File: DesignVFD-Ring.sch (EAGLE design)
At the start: 31 parts, among them IC1 LMR64010XMF/NOPB, IC2 LM340S-05, J1 NPPN081BFLD-RC, J2 NPPN081BFLD-RC, J3 NPPN081BFLD-RC, J4 NPPN081BFLD-RC, U1 MAX6920AWP+, U2 LM1084IS-5.0, U3 TPS76325DBVT

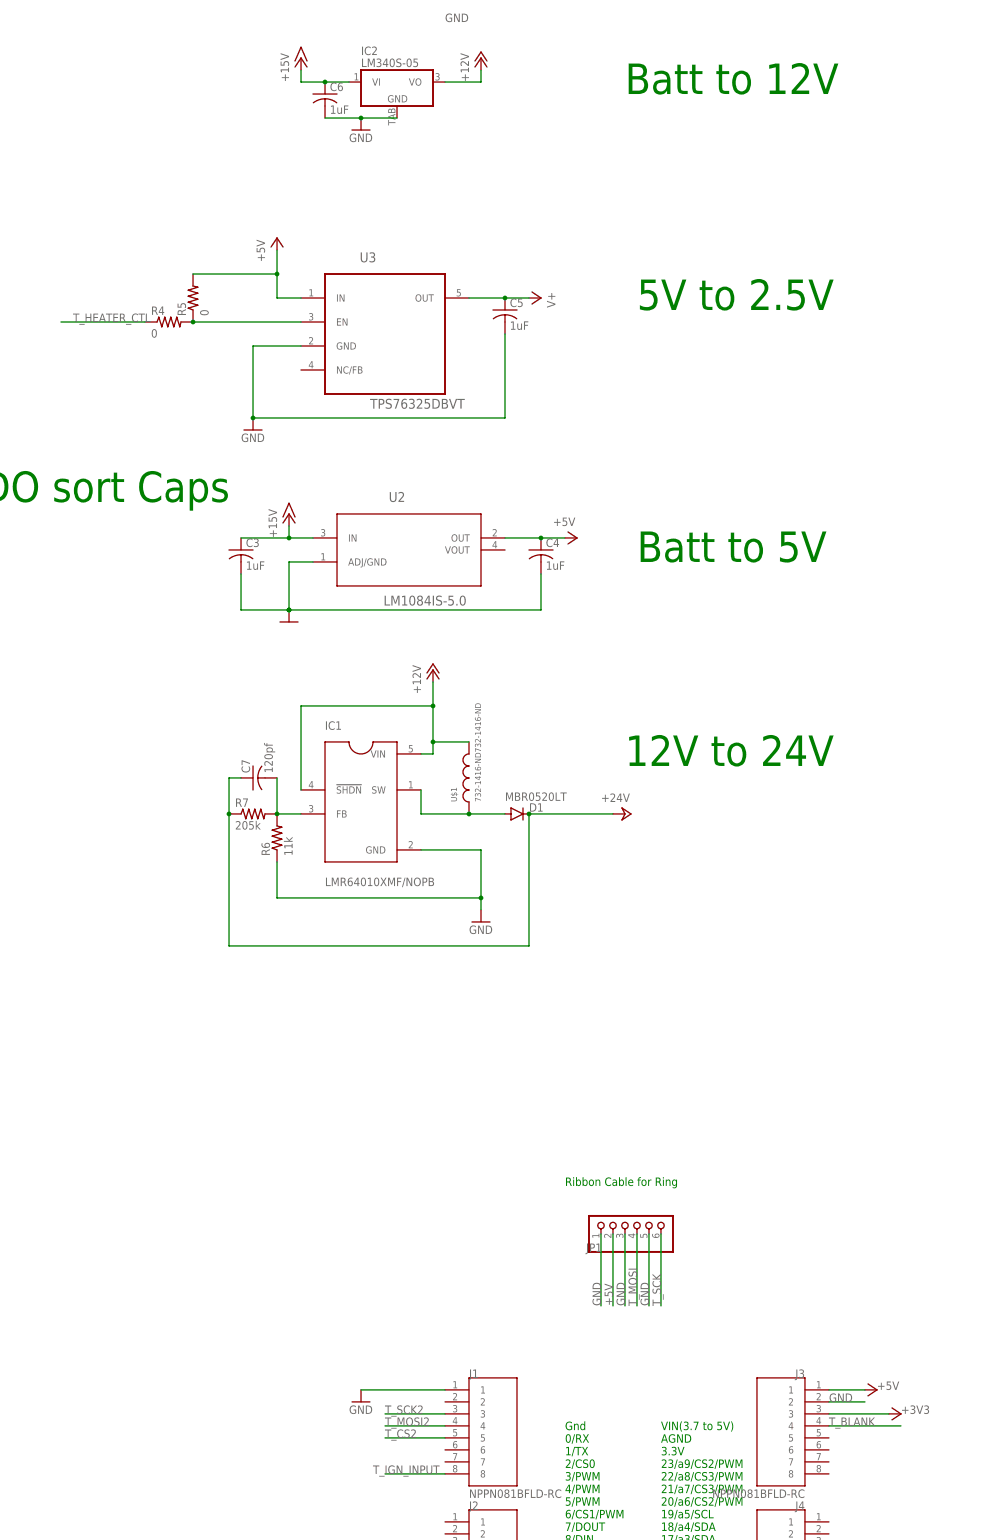
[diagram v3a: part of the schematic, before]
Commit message: added 7th ribbon cable connection, verified SMPS values
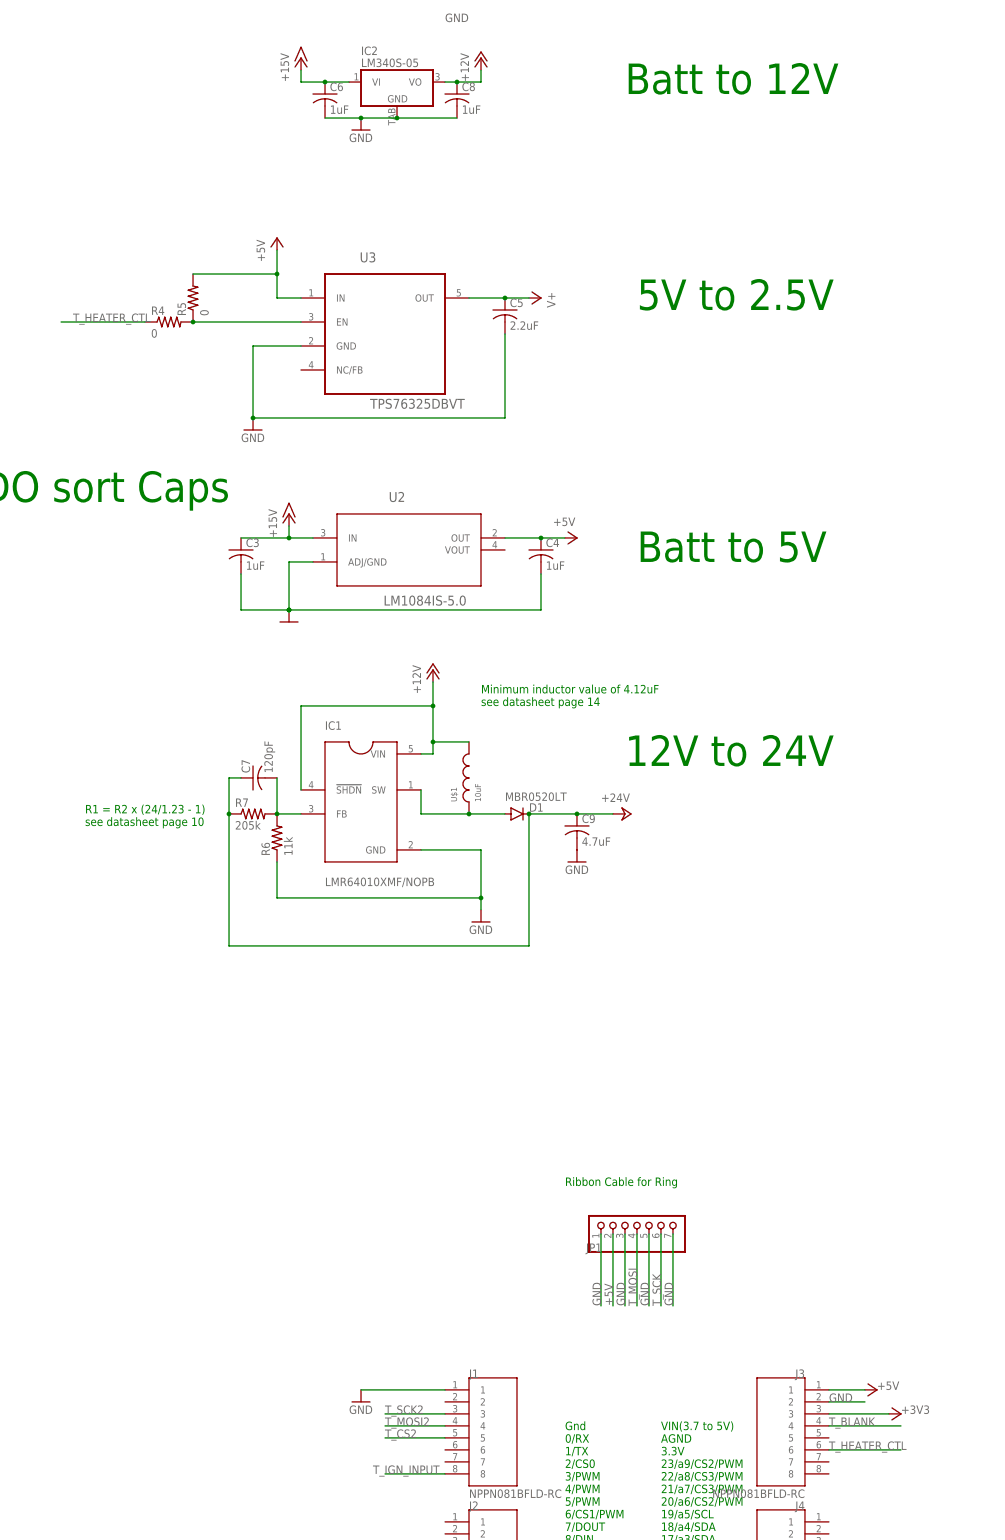
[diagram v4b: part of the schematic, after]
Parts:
- added C8: 1uF, rcl:C-USC0805
- added C9: 4.7uF, rcl:C-USC0805
- C5: value 1uF -> 2.2uF
- C7: value 120pf -> 120pF
- JP1: device pinhead:PINHD-1X6 -> pinhead:PINHD-1X7
- U$1: value 732-1416-ND732-1416-ND -> 10uF
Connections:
- net +12V: now also C8.1
- net +24V: now also C9.1
- net GND: now also C8.2, C9.2, JP1.7
- net T_HEATER_CTL: now also J3.6
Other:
- note added: "Minimum inductor value of 4.12uF see datasheet page 14"
- note added: "R1 = R2 x (24/1.23 - 1) see datasheet page 10"
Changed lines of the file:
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@@
 <part name="J3" library="NPPN081BFLD-RC" deviceset="NPPN081BFLD-RC" device=""/>
 <part name="J4" library="NPPN081BFLD-RC" deviceset="NPPN081BFLD-RC" device=""/>
-<part name="JP1" library="pinhead" library_urn="urn:adsk.eagle:library:325" deviceset="PINHD-1X6" device="" package3d_urn="urn:adsk.eagle:package:22472/2"/>
+<part name="JP1" library="pinhead" library_urn="urn:adsk.eagle:library:325" deviceset="PINHD-1X7" device="" package3d_urn="urn:adsk.eagle:package:22477/2"/>
 <part name="IC1" library="LMR64010XMF_NOPB" deviceset="LMR64010XMF/NOPB" device=""/>
 <part name="U1" library="MAX6920AWP_" deviceset="MAX6920AWP+" device=""/>
 <part name="D1" library="diode" library_urn="urn:adsk.eagle:library:210" deviceset="MBR0520LT" device="" package3d_urn="urn:adsk.eagle:package:43420/1"/>
-<part name="U$1" library="FormE" deviceset="732-1416-ND" device="732-1416-ND"/>
+<part name="U$1" library="FormE" deviceset="732-1416-ND" device="732-1416-ND" value="10uF"/>
 <part name="U2" library="LM1084IS-5.0" deviceset="LM1084IS-5.0" device=""/>
 <part name="U3" library="TPS76325DBVT" deviceset="TPS76325DBVT" device=""/>
@@
 <part name="C3" library="rcl" library_urn="urn:adsk.eagle:library:334" deviceset="C-US" device="C0805" package3d_urn="urn:adsk.eagle:package:23617/2" value="1uF"/>
 <part name="C4" library="rcl" library_urn="urn:adsk.eagle:library:334" deviceset="C-US" device="C0805" package3d_urn="urn:adsk.eagle:package:23617/2" value="1uF"/>
-<part name="C5" library="rcl" library_urn="urn:adsk.eagle:library:334" deviceset="C-US" device="C0805" package3d_urn="urn:adsk.eagle:package:23617/2" value="1uF"/>
+<part name="C5" library="rcl" library_urn="urn:adsk.eagle:library:334" deviceset="C-US" device="C0805" package3d_urn="urn:adsk.eagle:package:23617/2" value="2.2uF"/>
 <part name="IC2" library="linear" library_urn="urn:adsk.eagle:library:262" deviceset="LM340?-*" device="S" package3d_urn="urn:adsk.eagle:package:16425/2" technology="05"/>
 <part name="P+5" library="supply1" library_urn="urn:adsk.eagle:library:371" deviceset="+15V" device=""/>
@@
 <part name="R6" library="rcl" library_urn="urn:adsk.eagle:library:334" deviceset="R-US_" device="R0805" package3d_urn="urn:adsk.eagle:package:23553/2" value="11k"/>
 <part name="R7" library="rcl" library_urn="urn:adsk.eagle:library:334" deviceset="R-US_" device="R0805" package3d_urn="urn:adsk.eagle:package:23553/2" value="205k"/>
-<part name="C7" library="rcl" library_urn="urn:adsk.eagle:library:334" deviceset="C-US" device="C0805" package3d_urn="urn:adsk.eagle:package:23617/2" value="120pf"/>
+<part name="C7" library="rcl" library_urn="urn:adsk.eagle:library:334" deviceset="C-US" device="C0805" package3d_urn="urn:adsk.eagle:package:23617/2" value="120pF"/>
 <part name="GND6" library="supply1" library_urn="urn:adsk.eagle:library:371" deviceset="GND" device=""/>
 <part name="GND7" library="supply1" library_urn="urn:adsk.eagle:library:371" deviceset="GND" device=""/>
@@
 <part name="P+9" library="supply1" library_urn="urn:adsk.eagle:library:371" deviceset="+24V" device=""/>
 <part name="+3V3" library="supply1" library_urn="urn:adsk.eagle:library:371" deviceset="+3V3" device=""/>
+<part name="C8" library="rcl" library_urn="urn:adsk.eagle:library:334" deviceset="C-US" device="C0805" package3d_urn="urn:adsk.eagle:package:23617/2" value="1uF"/>
+<part name="C9" library="rcl" library_urn="urn:adsk.eagle:library:334" deviceset="C-US" device="C0805" package3d_urn="urn:adsk.eagle:package:23617/2" value="4.7uF"/>
+<part name="GND10" library="supply1" library_urn="urn:adsk.eagle:library:371" deviceset="GND" device=""/>
 </parts>
 <sheets>
@@
 <text x="203.2" y="30.48" size="6.4516" layer="91">IVL2-7/5 VFD Display and driver</text>
 <text x="312.42" y="187.96" size="6.4516" layer="91">Light Sensor</text>
+<text x="-40.64" y="177.8" size="1.778" layer="91">R1 = R2 x (24/1.23 - 1)
+see datasheet page 10</text>
+<text x="43.18" y="203.2" size="1.778" layer="91">Minimum inductor value of 4.12uF
+see datasheet page 14</text>
 </plain>
 <instances>
@@
 <instance part="+3V3" gate="G$1" x="246.38" y="99.06" smashed="yes" rot="R270">
 <attribute name="VALUE" x="238.76" y="96.52" size="1.778" layer="96"/>
+</instance>
+<instance part="C8" gate="G$1" x="38.1" y="332.74" smashed="yes">
+<attribute name="NAME" x="39.116" y="333.375" size="1.778" layer="95"/>
+<attribute name="VALUE" x="39.116" y="328.549" size="1.778" layer="96"/>
+</instance>
+<instance part="C9" gate="G$1" x="63.5" y="177.8" smashed="yes">
+<attribute name="NAME" x="64.516" y="178.435" size="1.778" layer="95"/>
+<attribute name="VALUE" x="64.516" y="173.609" size="1.778" layer="96"/>
+</instance>
+<instance part="GND10" gate="1" x="63.5" y="170.18" smashed="yes">
+<attribute name="VALUE" x="60.96" y="167.64" size="1.778" layer="96"/>
 </instance>
 </instances>
@@
 <wire x1="17.78" y1="327.66" x2="25.4" y2="327.66" width="0.1524" layer="91"/>
 <junction x="17.78" y="327.66"/>
+<pinref part="C8" gate="G$1" pin="2"/>
+<wire x1="25.4" y1="327.66" x2="38.1" y2="327.66" width="0.1524" layer="91"/>
+<junction x="25.4" y="327.66"/>
 </segment>
 <segment>
@@
 <label x="116.84" y="55.88" size="1.778" layer="95"/>
 </segment>
+<segment>
+<pinref part="JP1" gate="A" pin="7"/>
+<wire x1="83.82" y1="91.44" x2="83.82" y2="76.2" width="0.1524" layer="91"/>
+<label x="83.82" y="76.2" size="1.778" layer="95" rot="R90"/>
+</segment>
+<segment>
+<pinref part="C9" gate="G$1" pin="2"/>
+<pinref part="GND10" gate="1" pin="GND"/>
+</segment>
 </net>
 <net name="T_IGN_INPUT" class="0">
@@
 <label x="-43.18" y="284.48" size="1.778" layer="95"/>
 </segment>
+<segment>
+<pinref part="J3" gate="G$1" pin="6"/>
+<wire x1="116.84" y1="45.72" x2="132.08" y2="45.72" width="0.1524" layer="91"/>
+<label x="116.84" y="45.72" size="1.778" layer="95"/>
+</segment>
 </net>
 <net name="+15V" class="0">
@@
 <wire x1="43.18" y1="337.82" x2="43.18" y2="335.28" width="0.1524" layer="91"/>
 <pinref part="IC2" gate="A" pin="VO"/>
-<wire x1="35.56" y1="335.28" x2="43.18" y2="335.28" width="0.1524" layer="91"/>
+<wire x1="35.56" y1="335.28" x2="38.1" y2="335.28" width="0.1524" layer="91"/>
+<pinref part="C8" gate="G$1" pin="1"/>
+<wire x1="38.1" y1="335.28" x2="43.18" y2="335.28" width="0.1524" layer="91"/>
+<junction x="38.1" y="335.28"/>
 </segment>
 <segment>
@@
 <wire x1="33.02" y1="195.58" x2="40.64" y2="195.58" width="0.1524" layer="91"/>
 <junction x="33.02" y="195.58"/>
-<pinref part="IC1" gate="G$1" pin="!SHDN"/>
-<wire x1="5.08" y1="185.42" x2="5.08" y2="203.2" width="0.1524" layer="91"/>
 <wire x1="5.08" y1="203.2" x2="33.02" y2="203.2" width="0.1524" layer="91"/>
 <junction x="33.02" y="203.2"/>
+<pinref part="IC1" gate="G$1" pin="!SHDN"/>
+<wire x1="5.08" y1="203.2" x2="5.08" y2="185.42" width="0.1524" layer="91"/>
 </segment>
 </net>
@@
 <junction x="-10.16" y="180.34"/>
 <pinref part="P+8" gate="1" pin="+24V"/>
-<wire x1="53.34" y1="180.34" x2="71.12" y2="180.34" width="0.1524" layer="91"/>
+<wire x1="53.34" y1="180.34" x2="63.5" y2="180.34" width="0.1524" layer="91"/>
 <junction x="53.34" y="180.34"/>
-</segment>
-<segment>
+<pinref part="C9" gate="G$1" pin="1"/>
+<wire x1="63.5" y1="180.34" x2="71.12" y2="180.34" width="0.1524" layer="91"/>
+<junction x="63.5" y="180.34"/>
+</segment>
+<segment>

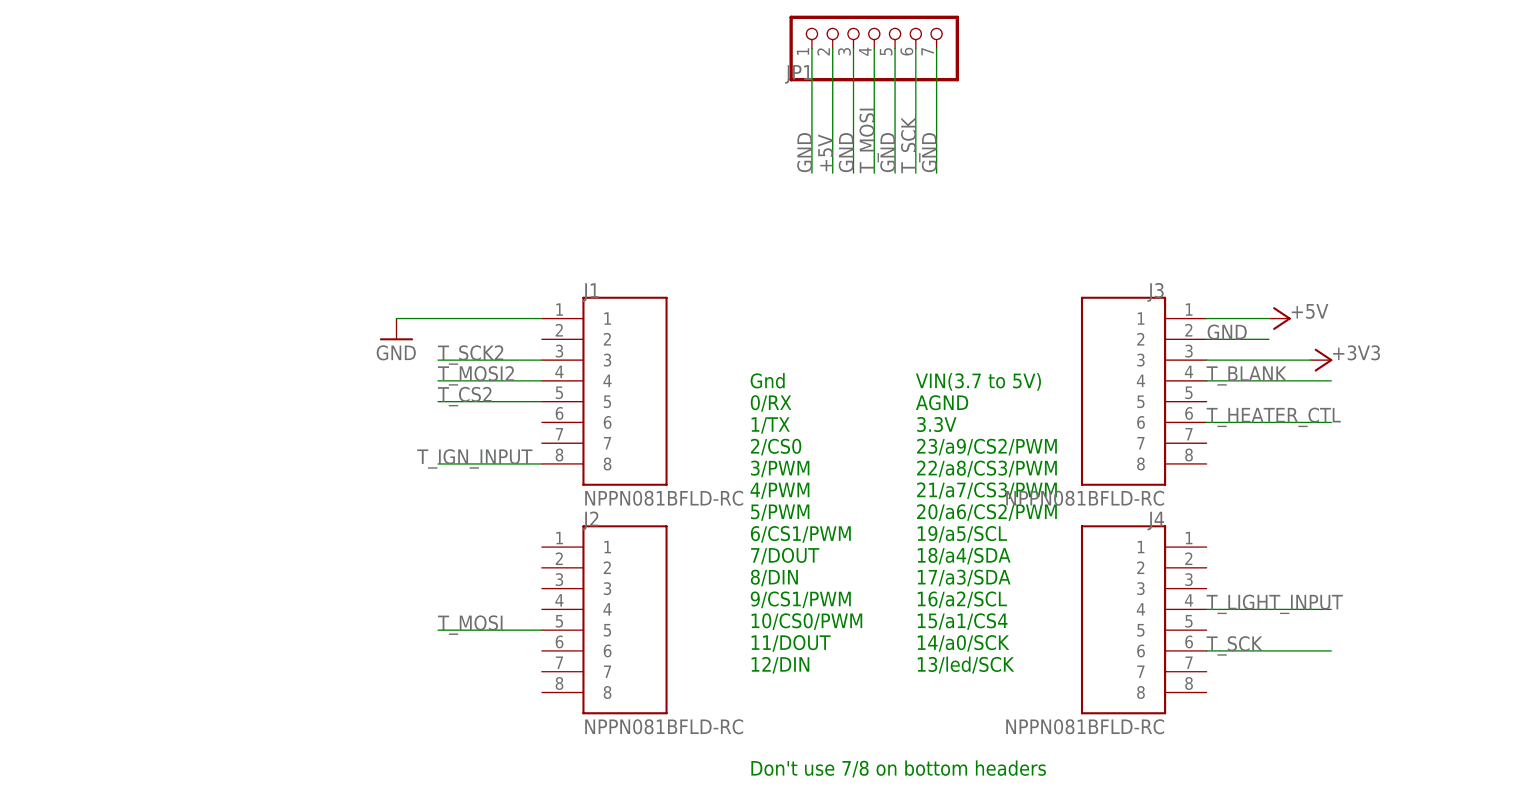
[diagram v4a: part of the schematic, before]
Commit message: Replaced headers with Teensy device
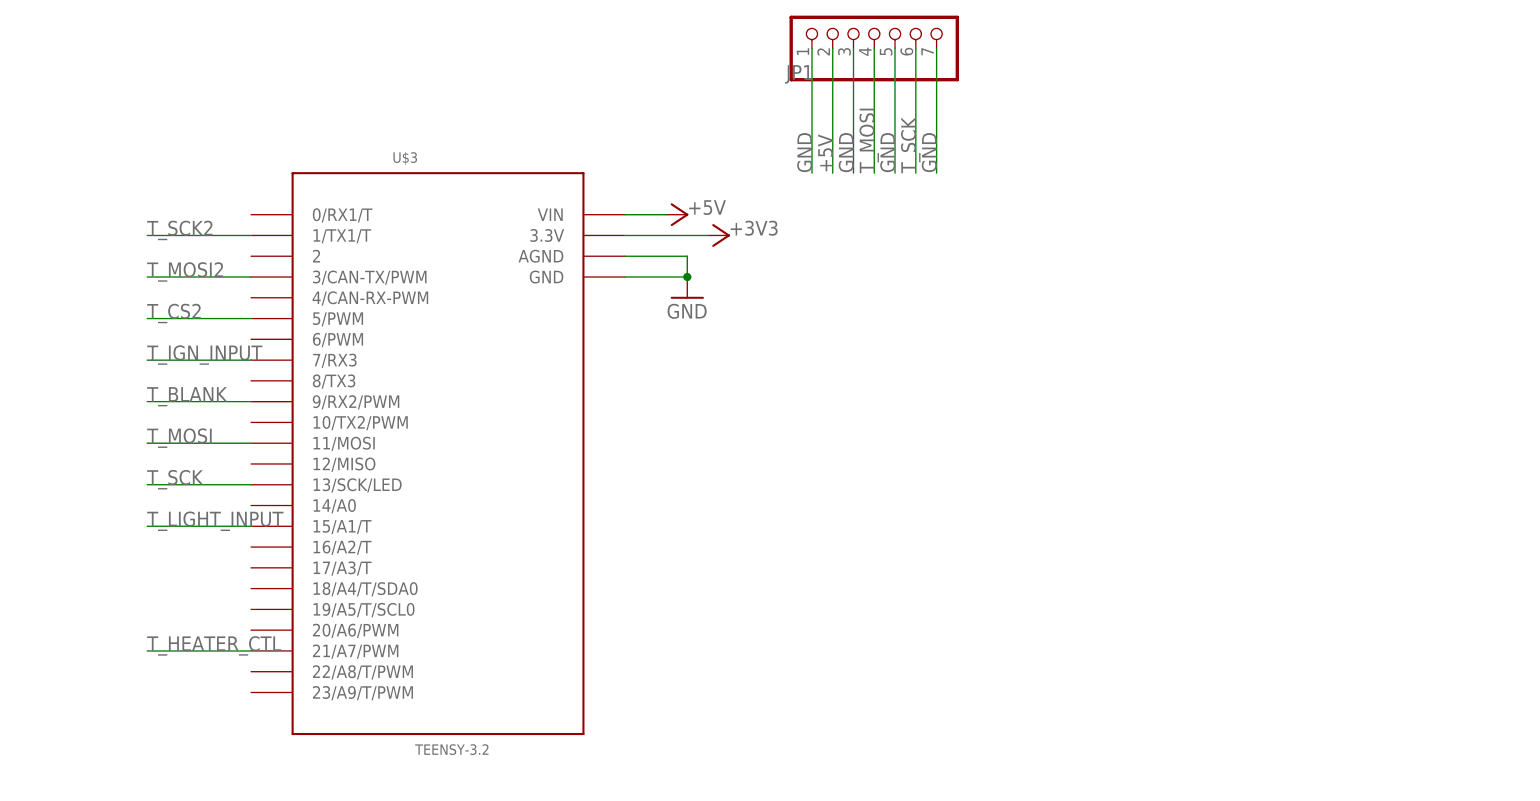
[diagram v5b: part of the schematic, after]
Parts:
- removed J1, J2, J3, J4: NPPN081BFLD-RC, NPPN081BFLD-RC:NPPN081BFLD-RC
- added U$3: TEENSY-3.2, FormE:TEENSY-3.2
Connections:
- net +3V3: now also U$3.3.3V; no longer J3.3
- net +5V: now also U$3.VIN; no longer J3.1
- net GND: now also U$3.AGND, U$3.GND; no longer J1.1, J3.2
- net T_BLANK: now also U$3.9/RX2/PWM; no longer J3.4
- net T_CS2: now also U$3.5/PWM; no longer J1.5
- net T_HEATER_CTL: now also U$3.21/A7/PWM; no longer J3.6
- net T_IGN_INPUT: now also U$3.7/RX3; no longer J1.8
- net T_LIGHT_INPUT: now also U$3.15/A1/T; no longer J4.4
- net T_MOSI: now also U$3.11/MOSI; no longer J2.5
- net T_MOSI2: now also U$3.3/CAN-TX/PWM; no longer J1.4
- net T_SCK: now also U$3.13/SCK/LED; no longer J4.6
- net T_SCK2: now also U$3.1/TX1/T; no longer J1.3
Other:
- note removed: "Don't use 7/8 on bottom headers"
- note removed: "Gnd 0/RX 1/TX 2/CS0 3/PWM 4/PWM 5/PWM 6/CS1/PWM 7/DOUT 8/DIN 9/CS1/PWM 10/CS0/PWM 11/DOUT 12/DIN"
- note removed: "VIN(3.7 to 5V) AGND 3.3V 23/a9/CS2/PWM 22/a8/CS3/PWM 21/a7/CS3/PWM 20/a6/CS2/PWM 19/a5/SCL 18/a4/SDA 17/a3/SDA 16/a2/SCL 15/a1/CS4 14/a0/SCK 13/led/SCK"
